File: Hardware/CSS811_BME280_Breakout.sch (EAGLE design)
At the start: 27 parts, among them J1 Qwiic Right Angle, J2 CCS811 Options, J3 Qwiic Right Angle, J4 PTH, U2 CCS811, U3 BME280

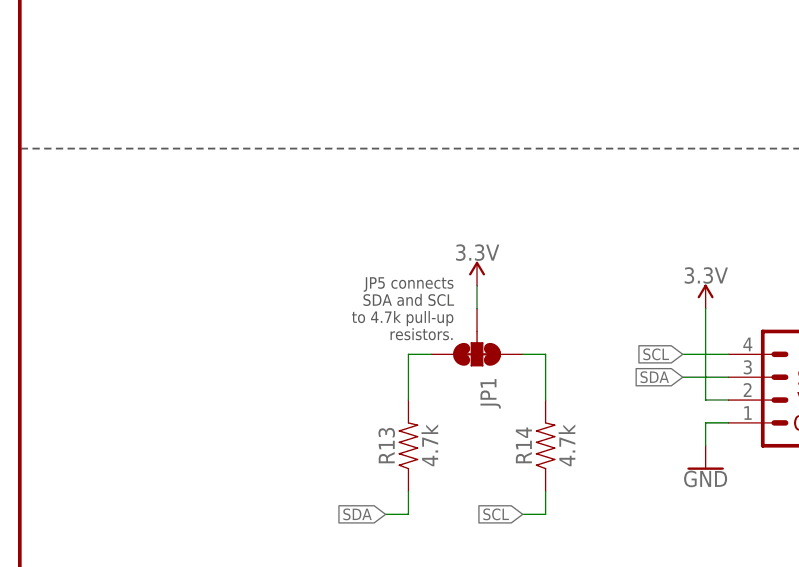
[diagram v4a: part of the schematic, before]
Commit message: Post design review aesthetic changes
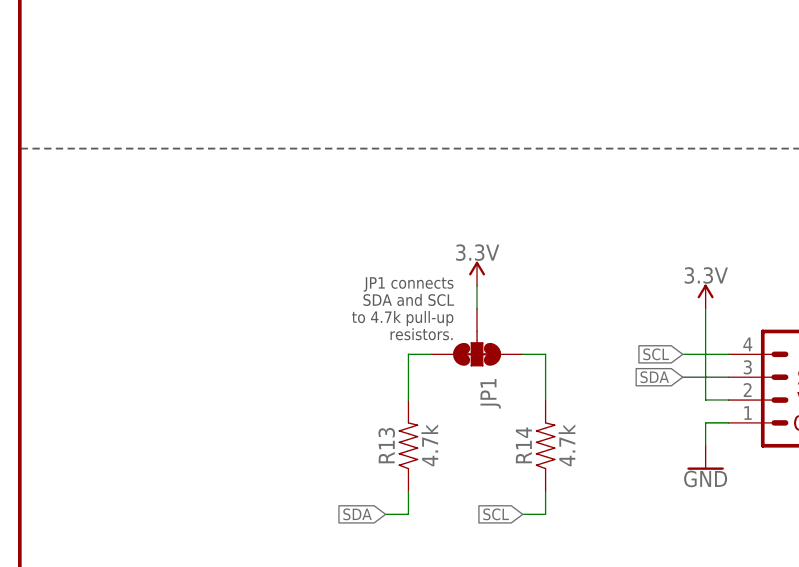
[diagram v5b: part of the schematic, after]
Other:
- note added: "JP1 connects SDA and SCL to 4.7k pull-up resistors."
- note removed: "JP5 connects SDA and SCL to 4.7k pull-up resistors."
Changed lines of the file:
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@@
 Open (Default) - 0x5B
 Closed - 0x5A</text>
-<text x="48.26" y="66.04" size="1.27" layer="97" align="center-right">JP5 connects
+<text x="48.26" y="66.04" size="1.27" layer="97" align="center-right">JP1 connects
 SDA and SCL
 to 4.7k pull-up

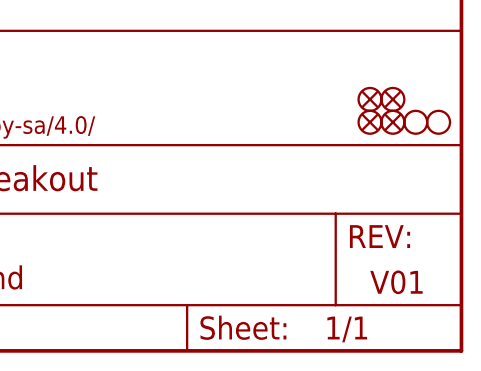
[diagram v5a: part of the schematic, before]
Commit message: updated silk for Reds
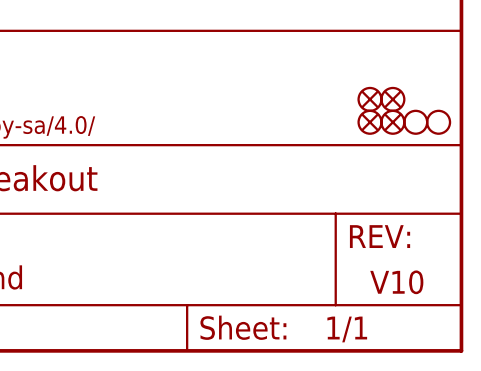
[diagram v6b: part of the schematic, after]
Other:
- note added: "V10"
- note removed: "V01"
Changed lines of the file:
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@@
 to 4.7k pull-up
 resistors.</text>
-<text x="238.76" y="7.62" size="2.54" layer="94" align="center-left">V01</text>
+<text x="238.76" y="7.62" size="2.54" layer="94" align="center-left">V10</text>
 <text x="170.688" y="12.446" size="2.54" layer="94" align="center-left">Nathan Seidle</text>
 <text x="214.376" y="120.396" size="1.27" layer="97" align="top-left">ADR2 sets the I2C address
